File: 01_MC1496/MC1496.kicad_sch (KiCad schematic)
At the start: 15 parts

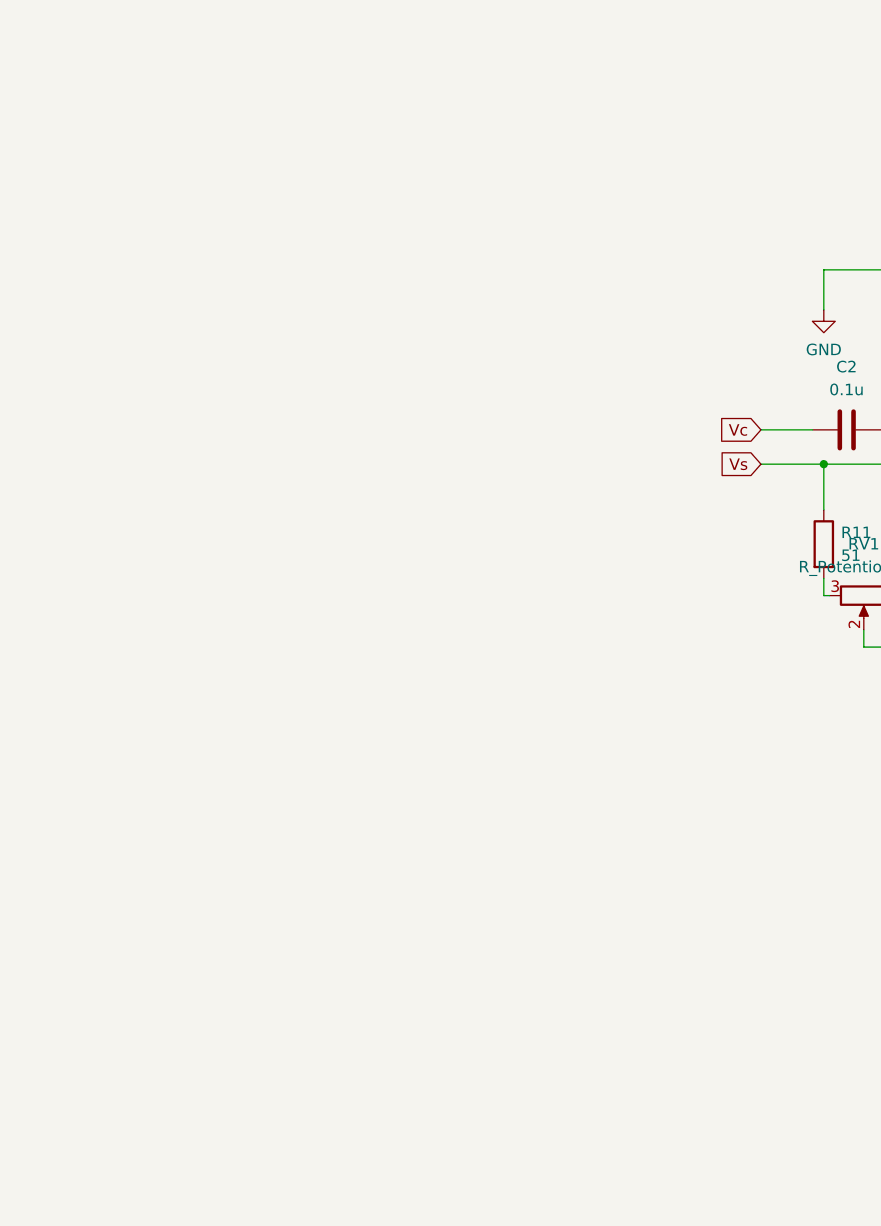
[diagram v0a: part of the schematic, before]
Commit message: マイク端子とアンプ
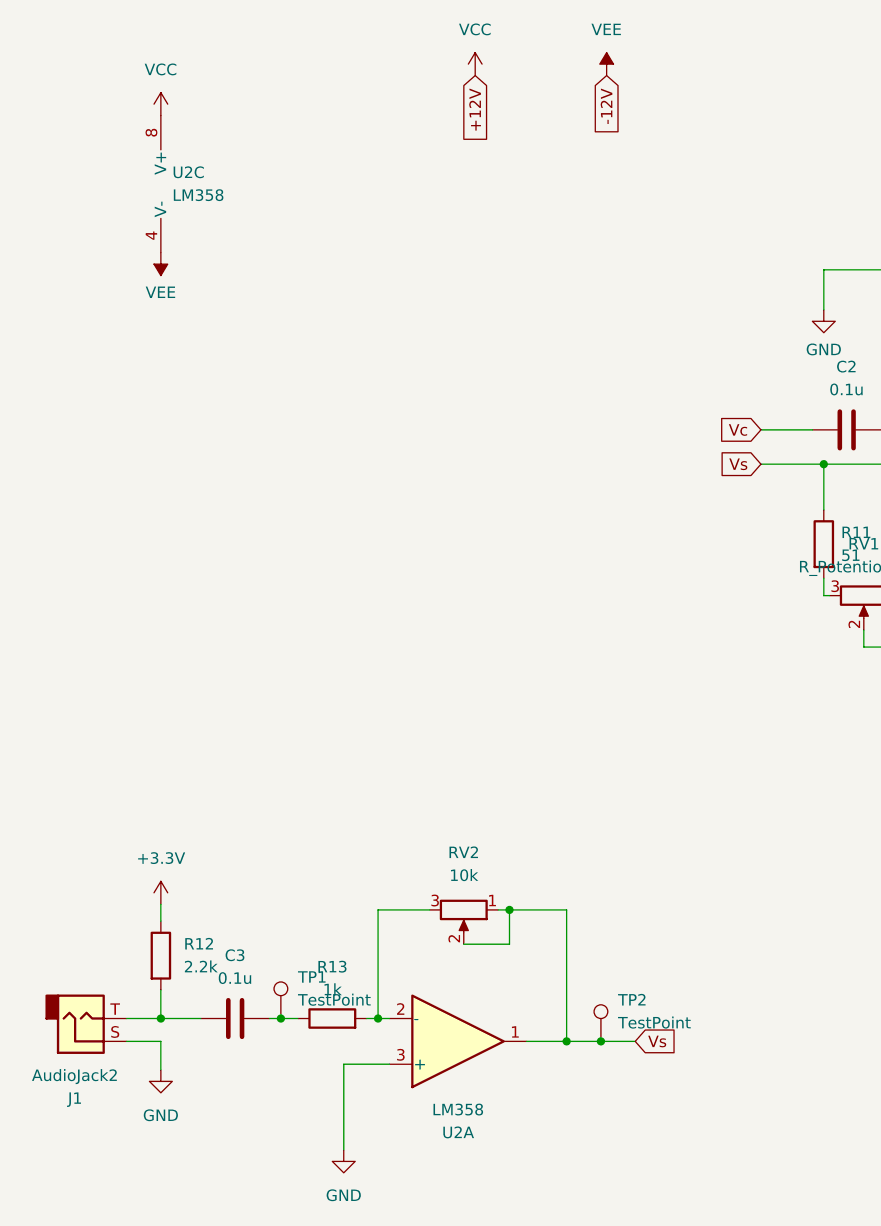
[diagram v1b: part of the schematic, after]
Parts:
- added C3: 0.1u, symbol Device:C
- added J1: AudioJack2, symbol Connector_Audio:AudioJack2
- added R12: 2.2k, symbol Device:R
- added R13: 1k, symbol Device:R
- added RV2: 10k, symbol Device:R_Potentiometer
- added TP1, TP2: TestPoint, symbol Connector:TestPoint
- added U2: LM358, symbol Amplifier_Operational:LM358
- U1: footprint Package_SO:SOIC-14_3.9x8.7mm_P1.27mm -> (none)
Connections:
- net GND: now also J1.S, U2.3 (+)
- net VCC: now also U2.8 (V+)
- net VEE: now also U2.4 (V-)
- net Vs: now also RV2.1, RV2.2, TP2.1, U2.1
- new net: R13.2, RV2.3, U2.2 (-)
- new net: C3.1, J1.T, R12.2
- new net: C3.2, R13.1, TP1.1
- new net +3.3V: R12.1

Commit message: SeeedXiao配置
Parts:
- added C4, C5: 0.1u, symbol Device:C
- added C6, C7: 100u, symbol Device:C_Polarized
- added R14: 10k, Resistor_SMD:R_0603_1608Metric, symbol Device:R
- added R15: 1k, Resistor_SMD:R_0603_1608Metric, symbol Device:R
- added TP3, TP4, TP5, TP6, TP7: TestPoint, symbol Connector:TestPoint
- added U3: SeeeduinoXIAO, 01_MC1496:Seeeduino XIAO-MOUDLE14P-2.54-21X17.8MM, symbol 01_Seeeduino XIAO:SeeeduinoXIAO
- added U4: L7805, Package_TO_SOT_THT:TO-220-3_Vertical, symbol Regulator_Linear:L7805
- R12, R13: footprint (none) -> Resistor_SMD:R_0603_1608Metric
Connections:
- net +3.3V: now also U3.12 (3V3)
- net GND: now also C4.2, C5.1, C6.2, C7.2, R15.2, TP5.1, TP6.1, TP7.1, U3.13 (GND), U4.2 (GND)
- net VCC: now also C4.1, C6.1, TP3.1, U4.1 (IN)
- net VEE: now also C5.2, TP4.1
- net Vc: now also R14.2, R15.1
- new net: R14.1, U3.2 (PA4_A1_D1)
- new net +5V: C7.1, U3.14 (5V), U4.3 (OUT)
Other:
- note added: "MC1496の推奨入力300mVに合わせて 3.3Vから1/11に降圧"
- note added: "シンボルとフットプリントを3端子レギュレータで代用しているが 3pinのDC/DCコンバータを使用"
- note added: "変調度調整用"

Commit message: 仮配置
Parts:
- added TP8: TestPoint, TestPoint:TestPoint_THTPad_D2.5mm_Drill1.2mm, symbol Connector:TestPoint
- C3: footprint (none) -> Capacitor_SMD:C_0603_1608Metric
- C4, C5: value 0.1u -> 1u; footprint (none) -> Capacitor_SMD:C_1206_3216Metric
- C6, C7: footprint (none) -> Capacitor_THT:CP_Radial_D6.3mm_P2.50mm
- J1: footprint (none) -> Connector_Audio:Jack_3.5mm_CUI_SJ1-3533NG_Horizontal
- R10, R11, R7, R8, R9: value 51 -> 47
- R14: value 10k -> 4.7k
- R15: value 1k -> 4.7k
- R2: value 6.8k -> 10k
- R3, R4: value 3.9k -> 4.7k
- RV1, RV2: footprint (none) -> Connector_PinHeader_2.54mm:PinHeader_1x03_P2.54mm_Vertical
- TP1, TP2, TP3, TP4, TP5, TP6, TP7: footprint (none) -> TestPoint:TestPoint_THTPad_D2.5mm_Drill1.2mm
- U1: value ~ -> MC1496; footprint (none) -> Package_SO:SOIC-14_3.9x8.7mm_P1.27mm
- U2: footprint (none) -> Package_SO:SOIC-8_3.9x4.9mm_P1.27mm
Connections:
- net +Vo: now also TP8.1
- net GND: now also R4.2; no longer R2.2
- net VCC: no longer R4.1
- net -V0: no longer names the net of U1.12 (Out)
- net -V0: no longer R4.2
- new net: R2.2, R4.1
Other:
- note added: "MC1496の推奨入力300mVrmsに合わせて 3.3Vから降圧"
- note added: "変調度調整用 5Vまで"
- note removed: "MC1496の推奨入力300mVに合わせて 3.3Vから1/11に降圧"
- note removed: "変調度調整用"

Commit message: 基板配置
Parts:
- added J2: Screw_Terminal_01x03, TerminalBlock:TerminalBlock_bornier-3_P5.08mm, symbol Connector:Screw_Terminal_01x03
- added J3: Screw_Terminal_01x02, TerminalBlock:TerminalBlock_bornier-2_P5.08mm, symbol Connector:Screw_Terminal_01x02
- J1: footprint Connector_Audio:Jack_3.5mm_CUI_SJ1-3533NG_Horizontal -> Connector_PinHeader_2.54mm:PinHeader_1x02_P2.54mm_Vertical
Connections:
- net +Vo: now also J3.1 (Pin_1)
- net GND: now also J1.1, J2.2 (Pin_2), J3.2 (Pin_2); no longer J1.S
- net VCC: now also J2.1 (Pin_1)
- net VEE: now also J2.3 (Pin_3)
- net at C3.1, R12.2: now also J1.2; no longer J1.T
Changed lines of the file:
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@@
+    (stroke (width 0) (type default))
+  )
+  (wire (pts (xy 176.53 48.895) (xy 178.435 48.895))
     (stroke (width 0) (type default))
   )
@@
   )
   (wire (pts (xy 110.49 95.25) (xy 110.49 100.33))
+    (stroke (width 0) (type default))
+  )
+  (wire (pts (xy 176.53 48.895) (xy 176.53 52.07))
     (stroke (width 0) (type default))
   )
@@
     )
   )
+  (global_label "-12V" (shape input) (at 53.34 97.155 0) (fields_autoplaced)
+    (effects (font (size 1.27 1.27)) (justify left))
+    (property "Intersheetrefs" "${INTERSHEET_REFS}" (at 61.4052 97.155 0)
+      (effects (font (size 1.27 1.27)) (justify left) hide)
+    )
+  )
+  (global_label "+12V" (shape input) (at 53.34 92.075 0) (fields_autoplaced)
+    (effects (font (size 1.27 1.27)) (justify left))
+    (property "Intersheetrefs" "${INTERSHEET_REFS}" (at 61.4052 92.075 0)
+      (effects (font (size 1.27 1.27)) (justify left) hide)
+    )
+  )
   (global_label "3V3" (shape input) (at 271.78 95.25 0) (fields_autoplaced)
     (effects (font (size 1.27 1.27)) (justify left))
@@
     (effects (font (size 1.27 1.27)) (justify right))
     (property "Intersheetrefs" "${INTERSHEET_REFS}" (at 71.755 60.1352 90)
+      (effects (font (size 1.27 1.27)) (justify right) hide)
+    )
+  )
+  (global_label "+Vo" (shape input) (at 178.435 46.355 180) (fields_autoplaced)
+    (effects (font (size 1.27 1.27)) (justify right))
+    (property "Intersheetrefs" "${INTERSHEET_REFS}" (at 171.6398 46.355 0)
       (effects (font (size 1.27 1.27)) (justify right) hide)
     )
@@
     )
   )
+  (symbol (lib_id "power:GND") (at 176.53 52.07 0) (unit 1)
+    (in_bom yes) (on_board yes) (dnp no) (fields_autoplaced)
+    (property "Reference" "#PWR023" (at 176.53 58.42 0)
+      (effects (font (size 1.27 1.27)) hide)
+    )
+    (property "Value" "GND" (at 176.53 56.515 0)
+      (effects (font (size 1.27 1.27)))
+    )
+    (property "Footprint" "" (at 176.53 52.07 0)
+      (effects (font (size 1.27 1.27)) hide)
+    )
+    (property "Datasheet" "" (at 176.53 52.07 0)
+      (effects (font (size 1.27 1.27)) hide)
+    )
+    (pin "1")
+    (instances
+      (project "MC1496"
+        (path "/ee06ee25-95a6-435c-9c3a-116077deac85"
+          (reference "#PWR023") (unit 1)
+        )
+      )
+    )
+  )
   (symbol (lib_id "power:GND") (at 110.49 78.105 0) (unit 1)
     (in_bom yes) (on_board yes) (dnp no) (fields_autoplaced)
@@
         (path "/ee06ee25-95a6-435c-9c3a-116077deac85"
           (reference "U4") (unit 1)
+        )
+      )
+    )
+  )
+  (symbol (lib_id "Connector:Screw_Terminal_01x02") (at 183.515 46.355 0) (unit 1)
+    (in_bom yes) (on_board yes) (dnp no) (fields_autoplaced)
+    (property "Reference" "J3" (at 186.69 46.355 0)
+      (effects (font (size 1.27 1.27)) (justify left))
+    )
+    (property "Value" "Screw_Terminal_01x02" (at 186.69 48.895 0)
+      (effects (font (size 1.27 1.27)) (justify left))
+    )
+    (property "Footprint" "TerminalBlock:TerminalBlock_bornier-2_P5.08mm" (at 183.515 46.355 0)
+      (effects (font (size 1.27 1.27)) hide)
+    )
+    (property "Datasheet" "~" (at 183.515 46.355 0)
+      (effects (font (size 1.27 1.27)) hide)
+    )
+    (pin "1")
+    (pin "2")
+    (instances
+      (project "MC1496"
+        (path "/ee06ee25-95a6-435c-9c3a-116077deac85"
+          (reference "J3") (unit 1)
         )
       )
@@
       (effects (font (size 1.27 1.27)))
     )
-    (property "Footprint" "Connector_Audio:Jack_3.5mm_CUI_SJ1-3533NG_Horizontal" (at 27.94 156.845 0)
+    (property "Footprint" "Connector_PinHeader_2.54mm:PinHeader_1x02_P2.54mm_Vertical" (at 27.94 156.845 0)
       (effects (font (size 1.27 1.27)) hide)
     )
@@
       (effects (font (size 1.27 1.27)) hide)
     )
-    (pin "S")
-    (pin "T")
+    (pin "1")
+    (pin "2")
     (instances
       (project "MC1496"
@@
         (path "/ee06ee25-95a6-435c-9c3a-116077deac85"
           (reference "#PWR04") (unit 1)
+        )
+      )
+    )
+  )
+  (symbol (lib_id "Connector:Screw_Terminal_01x03") (at 48.26 94.615 0) (mirror y) (unit 1)
+    (in_bom yes) (on_board yes) (dnp no)
+    (property "Reference" "J2" (at 48.26 102.87 0)
+      (effects (font (size 1.27 1.27)))
+    )
+    (property "Value" "Screw_Terminal_01x03" (at 48.26 100.33 0)
+      (effects (font (size 1.27 1.27)))
+    )
+    (property "Footprint" "TerminalBlock:TerminalBlock_bornier-3_P5.08mm" (at 48.26 94.615 0)
+      (effects (font (size 1.27 1.27)) hide)
+    )
+    (property "Datasheet" "~" (at 48.26 94.615 0)
+      (effects (font (size 1.27 1.27)) hide)
+    )
+    (pin "1")
+    (pin "2")
+    (pin "3")
+    (instances
+      (project "MC1496"
+        (path "/ee06ee25-95a6-435c-9c3a-116077deac85"
+          (reference "J2") (unit 1)
         )
       )
@@
         )
       )
+    )
+  )
+  (symbol (lib_id "power:GND") (at 53.34 94.615 90) (unit 1)
+    (in_bom yes) (on_board yes) (dnp no) (fields_autoplaced)
+    (property "Reference" "#PWR022" (at 59.69 94.615 0)
+      (effects (font (size 1.27 1.27)) hide)
+    )
+    (property "Value" "GND" (at 57.15 94.615 90)
+      (effects (font (size 1.27 1.27)) (justify right))
+    )
+    (property "Footprint" "" (at 53.34 94.615 0)
+      (effects (font (size 1.27 1.27)) hide)
+    )
+    (property "Datasheet" "" (at 53.34 94.615 0)
+      (effects (font (size 1.27 1.27)) hide)
+    )
+    (pin "1")
+    (instances
+      (project "MC1496"
+        (path "/ee06ee25-95a6-435c-9c3a-116077deac85"
+          (reference "#PWR022") (unit 1)
+        )
+      )

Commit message: TP名設定
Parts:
- added TP9: Vc, TestPoint:TestPoint_THTPad_D2.5mm_Drill1.2mm, symbol Connector:TestPoint
- TP1: value TestPoint -> MIC
- TP2: value TestPoint -> Vs
- TP3: value TestPoint -> +12V
- TP4: value TestPoint -> -12V
- TP5, TP6, TP7: value TestPoint -> GND
- TP8: value TestPoint -> +Vo
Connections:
- net at C2.1, R7.1, U1.10 (C_In): now also TP9.1
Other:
- note added: "40kHzを出力するマイコン"
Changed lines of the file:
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@@
 (kicad_sch (version 20230121) (generator eeschema)
   (paper "A4")
+  (junction (at 121.92 91.44) (diameter 0) (color 0 0 0 0)
+  )
   (junction (at 46.99 64.135) (diameter 0) (color 0 0 0 0)
   )
@@
     (stroke (width 0) (type default))
   )
+  (wire (pts (xy 121.92 91.44) (xy 138.43 91.44))
+    (stroke (width 0) (type default))
+  )
   (wire (pts (xy 59.69 156.845) (xy 60.96 156.845))
     (stroke (width 0) (type default))
@@
     (stroke (width 0) (type default))
   )
-  (wire (pts (xy 118.745 91.44) (xy 138.43 91.44))
+  (wire (pts (xy 118.745 91.44) (xy 121.92 91.44))
     (stroke (width 0) (type default))
   )
@@
   (text "MC1496の推奨入力300mVrmsに合わせて\n3.3Vから降圧" (at 196.215 77.47 0)
     (effects (font (face "BIZ UDゴシック") (size 1.27 1.27)) (justify left bottom))
+  )
+  (text "40kHzを出力するマイコン" (at 242.57 69.215 0)
+    (effects (font (size 1.27 1.27)) (justify left bottom))
   )
   (text "シンボルとフットプリントを3端子レギュレータで代用しているが\n3pinのDC/DCコンバータを使用" (at 208.28 138.43 0)
@@
       (effects (font (size 1.27 1.27)) (justify left))
     )
-    (property "Value" "TestPoint" (at 85.09 46.863 0)
+    (property "Value" "-12V" (at 85.09 46.863 0)
       (effects (font (size 1.27 1.27)) (justify left))
     )
@@
       (effects (font (size 1.27 1.27)) (justify left))
     )
-    (property "Value" "TestPoint" (at 74.93 65.913 0)
+    (property "Value" "GND" (at 74.93 65.913 0)
       (effects (font (size 1.27 1.27)) (justify left))
     )
@@
       (effects (font (size 1.27 1.27)) (justify left))
     )
-    (property "Value" "TestPoint" (at 77.47 65.913 0)
+    (property "Value" "GND" (at 77.47 65.913 0)
       (effects (font (size 1.27 1.27)) (justify left))
     )
@@
       (effects (font (size 1.27 1.27)) (justify left))
     )
-    (property "Value" "TestPoint" (at 180.34 89.408 0)
+    (property "Value" "+Vo" (at 180.34 89.408 0)
       (effects (font (size 1.27 1.27)) (justify left))
     )
@@
       (effects (font (size 1.27 1.27)) (justify left))
     )
-    (property "Value" "TestPoint" (at 69.85 46.863 0)
+    (property "Value" "+12V" (at 69.85 46.863 0)
       (effects (font (size 1.27 1.27)) (justify left))
     )
@@
     )
   )
+  (symbol (lib_id "Connector:TestPoint") (at 121.92 91.44 0) (unit 1)
+    (in_bom yes) (on_board yes) (dnp no) (fields_autoplaced)
+    (property "Reference" "TP9" (at 123.825 86.868 0)
+      (effects (font (size 1.27 1.27)) (justify left))
+    )
+    (property "Value" "Vc" (at 123.825 89.408 0)
+      (effects (font (size 1.27 1.27)) (justify left))
+    )
+    (property "Footprint" "TestPoint:TestPoint_THTPad_D2.5mm_Drill1.2mm" (at 127 91.44 0)
+      (effects (font (size 1.27 1.27)) hide)
+    )
+    (property "Datasheet" "~" (at 127 91.44 0)
+      (effects (font (size 1.27 1.27)) hide)
+    )
+    (pin "1")
+    (instances
+      (project "MC1496"
+        (path "/ee06ee25-95a6-435c-9c3a-116077deac85"
+          (reference "TP9") (unit 1)
+        )
+      )
+    )
+  )
   (symbol (lib_id "power:+3.3V") (at 36.83 144.145 0) (unit 1)
     (in_bom yes) (on_board yes) (dnp no) (fields_autoplaced)
@@
   (symbol (lib_id "Connector:TestPoint") (at 78.105 67.945 0) (unit 1)
     (in_bom yes) (on_board yes) (dnp no) (fields_autoplaced)
-    (property "Reference" "TP7" (at 80.645 63.373 0)
-      (effects (font (size 1.27 1.27)) (justify left))
-    )
-    (property "Value" "TestPoint" (at 80.645 65.913 0)
+    (property "Reference" "TP7" (at 80.01 63.373 0)
+      (effects (font (size 1.27 1.27)) (justify left))
+    )
+    (property "Value" "GND" (at 80.01 65.913 0)
       (effects (font (size 1.27 1.27)) (justify left))
     )
@@
       (effects (font (size 1.27 1.27)) (justify left))
     )
-    (property "Value" "TestPoint" (at 52.07 154.813 0)
+    (property "Value" "MIC" (at 52.07 154.813 0)
       (effects (font (size 1.27 1.27)) (justify left))
     )
@@
       (effects (font (size 1.27 1.27)) (justify left))
     )
-    (property "Value" "TestPoint" (at 87.63 157.353 0)
-      (effects (font (size 1.27 1.27)) (justify left))
-    )
+    (property "Value" "Vs" (at 87.63 157.353 0)
+      (effects (font (size 1.27 1.27)) (justify left))
+    )

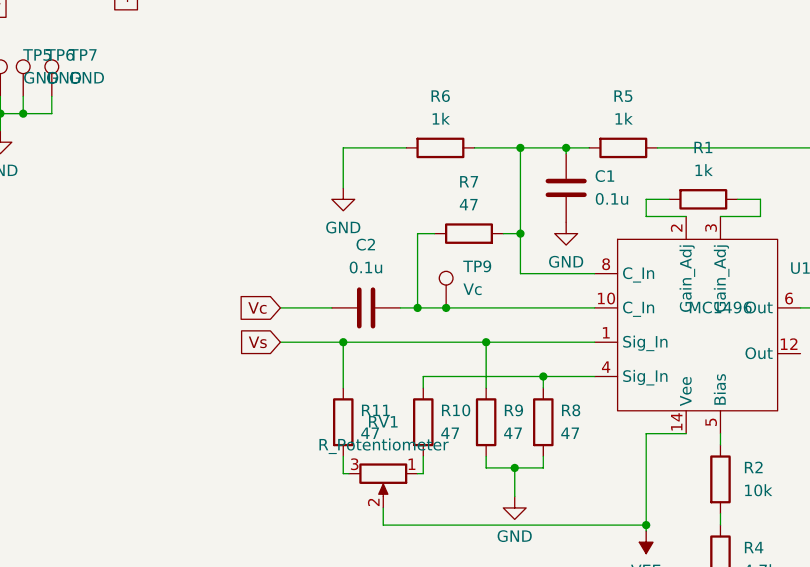
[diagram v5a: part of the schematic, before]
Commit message: VcとVc_ACのTP分割
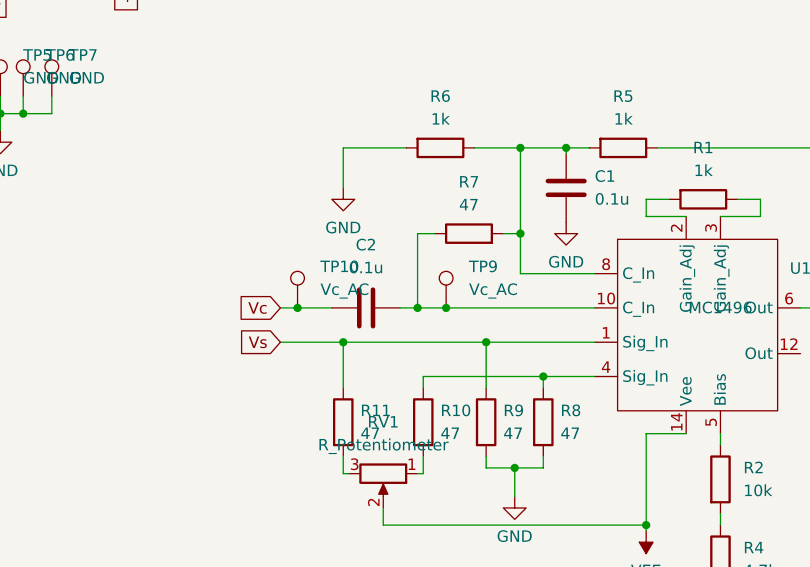
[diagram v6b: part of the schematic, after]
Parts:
- added TP10: Vc_AC, TestPoint:TestPoint_THTPad_D2.5mm_Drill1.2mm, symbol Connector:TestPoint
- TP9: value Vc -> Vc_AC
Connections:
- net Vc: now also TP10.1
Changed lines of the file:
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@@
   (junction (at 60.96 156.845) (diameter 0) (color 0 0 0 0)
   )
+  (junction (at 105.41 91.44) (diameter 0) (color 0 0 0 0)
+  )
   (junction (at 267.335 95.25) (diameter 0) (color 0 0 0 0)
   )
@@
     (stroke (width 0) (type default))
   )
+  (wire (pts (xy 105.41 91.44) (xy 109.22 91.44))
+    (stroke (width 0) (type default))
+  )
   (wire (pts (xy 257.175 87.63) (xy 259.08 87.63))
     (stroke (width 0) (type default))
@@
     (stroke (width 0) (type default))
   )
-  (wire (pts (xy 103.505 91.44) (xy 109.22 91.44))
+  (wire (pts (xy 103.505 91.44) (xy 105.41 91.44))
     (stroke (width 0) (type default))
   )
@@
     )
   )
+  (symbol (lib_id "Connector:TestPoint") (at 105.41 91.44 0) (unit 1)
+    (in_bom yes) (on_board yes) (dnp no) (fields_autoplaced)
+    (property "Reference" "TP10" (at 107.95 86.868 0)
+      (effects (font (size 1.27 1.27)) (justify left))
+    )
+    (property "Value" "Vc_AC" (at 107.95 89.408 0)
+      (effects (font (size 1.27 1.27)) (justify left))
+    )
+    (property "Footprint" "TestPoint:TestPoint_THTPad_D2.5mm_Drill1.2mm" (at 110.49 91.44 0)
+      (effects (font (size 1.27 1.27)) hide)
+    )
+    (property "Datasheet" "~" (at 110.49 91.44 0)
+      (effects (font (size 1.27 1.27)) hide)
+    )
+    (pin "1")
+    (instances
+      (project "MC1496"
+        (path "/ee06ee25-95a6-435c-9c3a-116077deac85"
+          (reference "TP10") (unit 1)
+        )
+      )
+    )
+  )
   (symbol (lib_id "power:VCC") (at 172.72 71.12 0) (unit 1)
     (in_bom yes) (on_board yes) (dnp no) (fields_autoplaced)
@@
   (symbol (lib_id "Connector:TestPoint") (at 121.92 91.44 0) (unit 1)
     (in_bom yes) (on_board yes) (dnp no) (fields_autoplaced)
-    (property "Reference" "TP9" (at 123.825 86.868 0)
-      (effects (font (size 1.27 1.27)) (justify left))
-    )
-    (property "Value" "Vc" (at 123.825 89.408 0)
-      (effects (font (size 1.27 1.27)) (justify left))
-    )
+    (property "Reference" "TP9" (at 124.46 86.868 0)
+      (effects (font (size 1.27 1.27)) (justify left))
+    )
+    (property "Value" "Vc_AC" (at 124.46 89.408 0)
+      (effects (font (size 1.27 1.27)) (justify left))
+    )
